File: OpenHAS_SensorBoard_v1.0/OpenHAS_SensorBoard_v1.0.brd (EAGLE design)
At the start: 37.5 x 47.6 mm, 18 parts, among them IC1 MCP1703CB, IC2 MCP9700SMD, IC3 TEMT6000, IC4 HIH-5030SMD, Q1 N-MOSFET

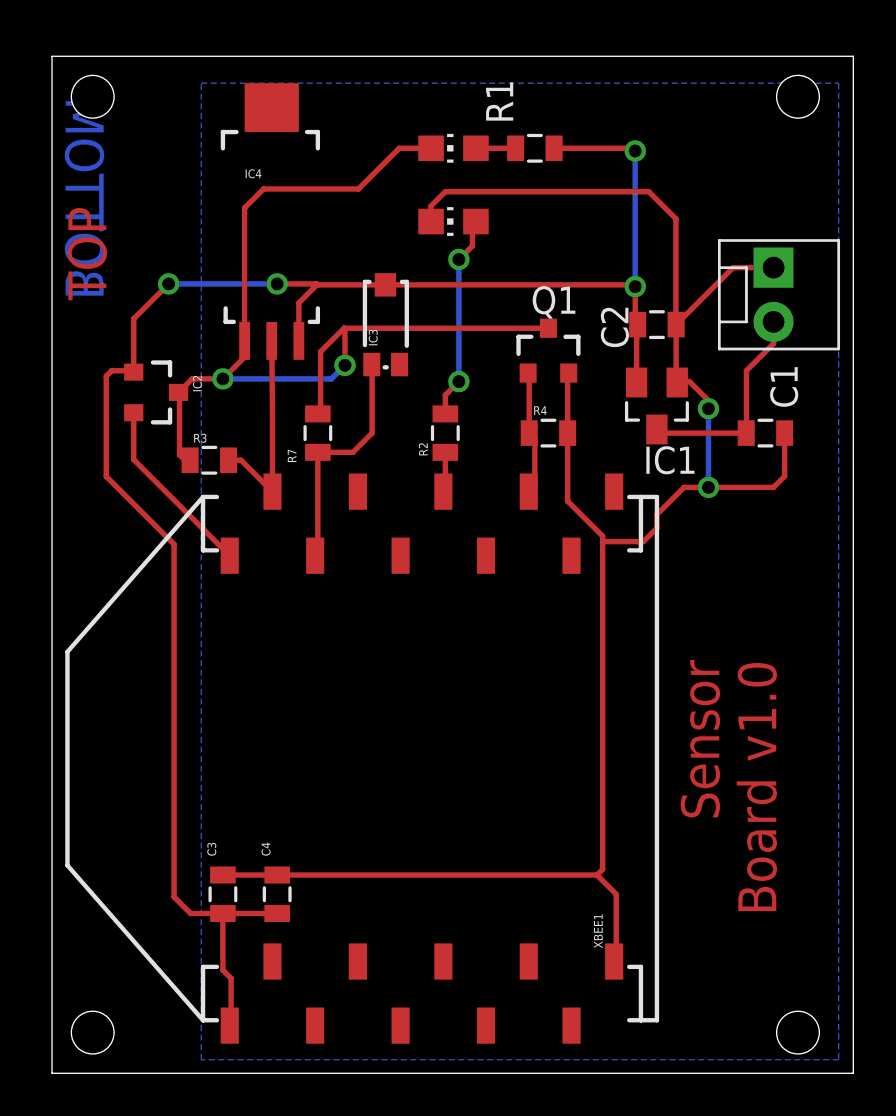
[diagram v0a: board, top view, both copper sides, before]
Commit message: Added voltage divider to the humidity sensor. Redesigned layout
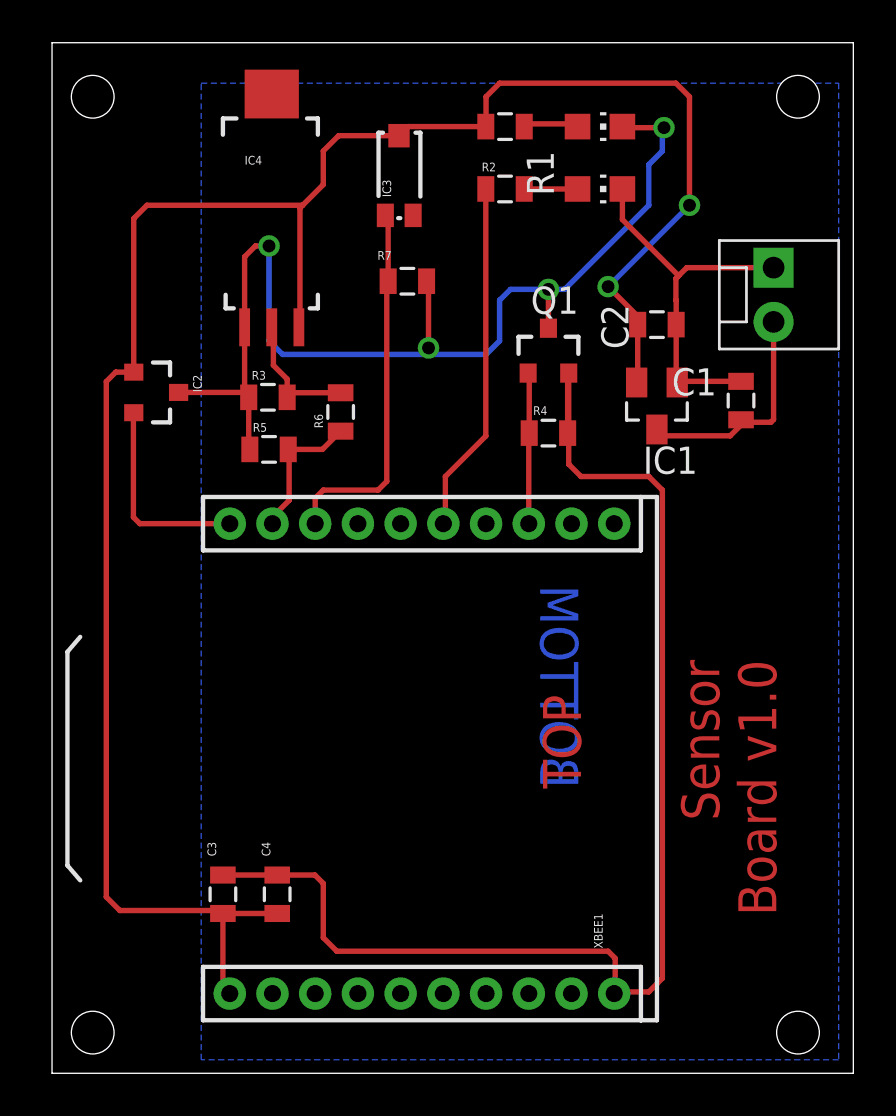
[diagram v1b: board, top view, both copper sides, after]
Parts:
- added R5: 5k, SparkFun-Resistors:0805
- added R6: 4.7k, SparkFun-Resistors:0805
- XBEE1: value XBEE-2B3 -> XBEE-2B2; device SparkFun-RF:XBEE-SMD -> SparkFun-RF:XBEE-SILK
- moved R2 11.8 mm to (21.2, 41.4), turned to 0 degrees
- moved R7 8.26 mm to (16.6, 37.1), turned to 180 degrees
- moved LED2 7.03 mm to (25.7, 41.4), turned to 270 degrees
- moved IC3 7.01 mm to (16.3, 42.0)
- moved LED1 6.93 mm to (25.7, 44.3), turned to 270 degrees
- moved R3 4.03 mm to (10.1, 31.6)
- moved C1 1.90 mm to (32.3, 31.5), turned to 90 degrees
- moved R1 1.73 mm to (21.2, 44.3), turned to 0 degrees
- moved IC4 0.64 mm to (10.3, 40.0)
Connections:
- new net N$3: IC4.2, R3.2, R6.2
- net HUMID: now also R5.2, R6.1; no longer IC4.2, R3.2
- net SW_GND: now also R5.1
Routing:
- net 3.3V: track 82.2 -> 97.0 mm, vias 4 -> 2
- net N$1: track 1.93 -> 16.5 mm
- net GND: track 91.0 -> 78.4 mm, vias 2 -> 0
- net N$2: track 9.37 -> 2.49 mm, vias 2 -> 0
- net LIGHT: track 11.0 -> 17.4 mm
- net N$3: track 0.00 -> 6.17 mm
- net SW_GND: track 46.0 -> 51.5 mm, vias 2 -> 4
- net HUMID: track 9.72 -> 6.62 mm
- net ACTIVE: track 5.85 -> 7.08 mm
- net TEMP: track 8.56 -> 9.54 mm
- net N$5: track 1.86 -> 2.60 mm
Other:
- board size 37.5 x 47.6 mm -> 37.5 x 48.2 mm
